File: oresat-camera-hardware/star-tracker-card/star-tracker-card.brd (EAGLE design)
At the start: 99.8 x 94.6 mm, 321 parts, among them J1 ORESAT-DEBUG-CONNECTOR-CARD, J100 DM3BT-DSF-PEJS, J101 3-1734592-64-1734592-0, J102 FTSH-105-XX-X-DV-K, J4 TFM-120-01-L-D-RA, Q1 MMBT2907, Q2 PMV45EN, Q3 DMP2240UDM, Q4 PMV45EN, Q5 MOSFET-PCH-SOT23-6, Q6 MOSFET-PCH-SOT23-6, U1 RCLAMP0504FB, U10 TLVH431, U11 TCAN330, U12 MIC842LYC5, U13 MIC842LYC5, U14 MAX4211FETE, U15 TPS62112, U16 MAX7310ATE, U17 25AAXX, U2 TPS2051CDBVR, U4 SN74LVC1G07DCK, U5 SN74LVC8T245MPWREPPW24-M, U6 CLVCH16T245MDGGREP, U7 OSD3358-512M-BSM, U8 TLV70028QDDCRQ1, U9 TCA9509DGKRDGK8-M, Y1 24MHz, Y2 ABS07-32.768KHZ-T

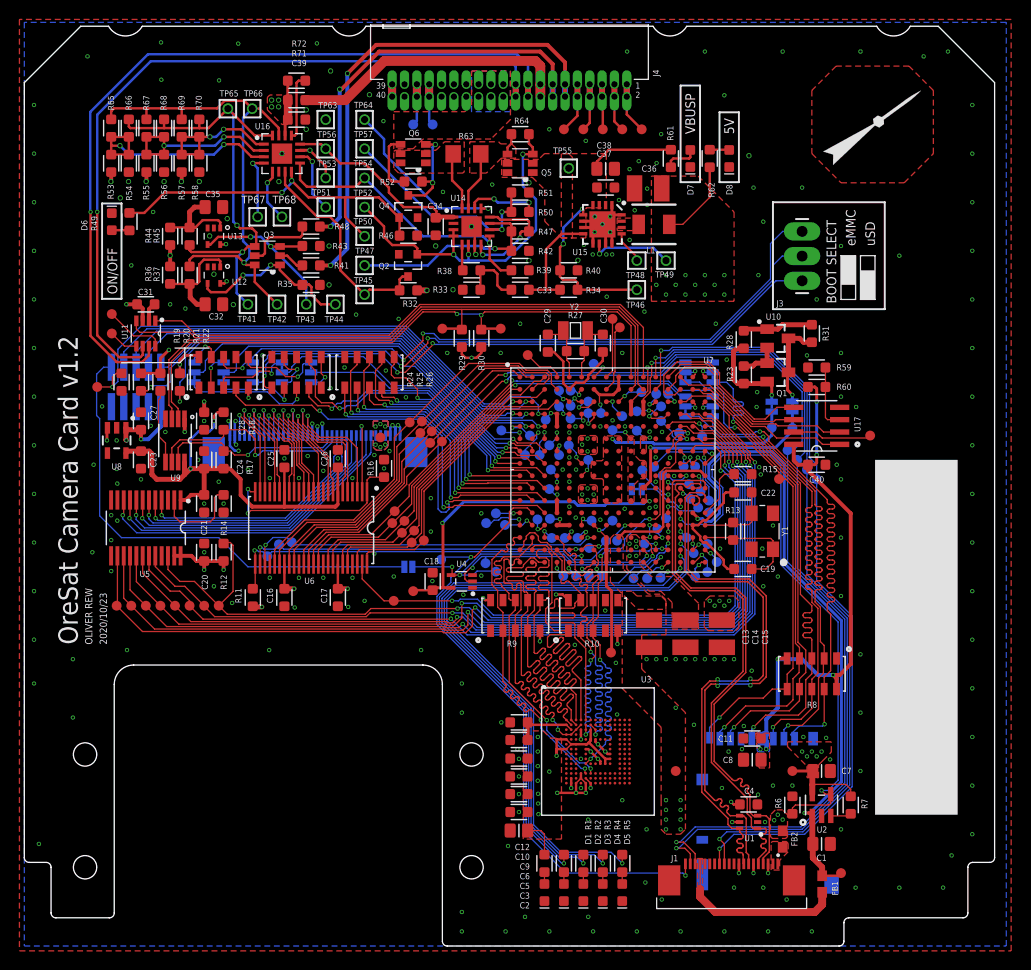
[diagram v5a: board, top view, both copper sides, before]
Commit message: added ESD protection to I2C0 and EEPROM_WP
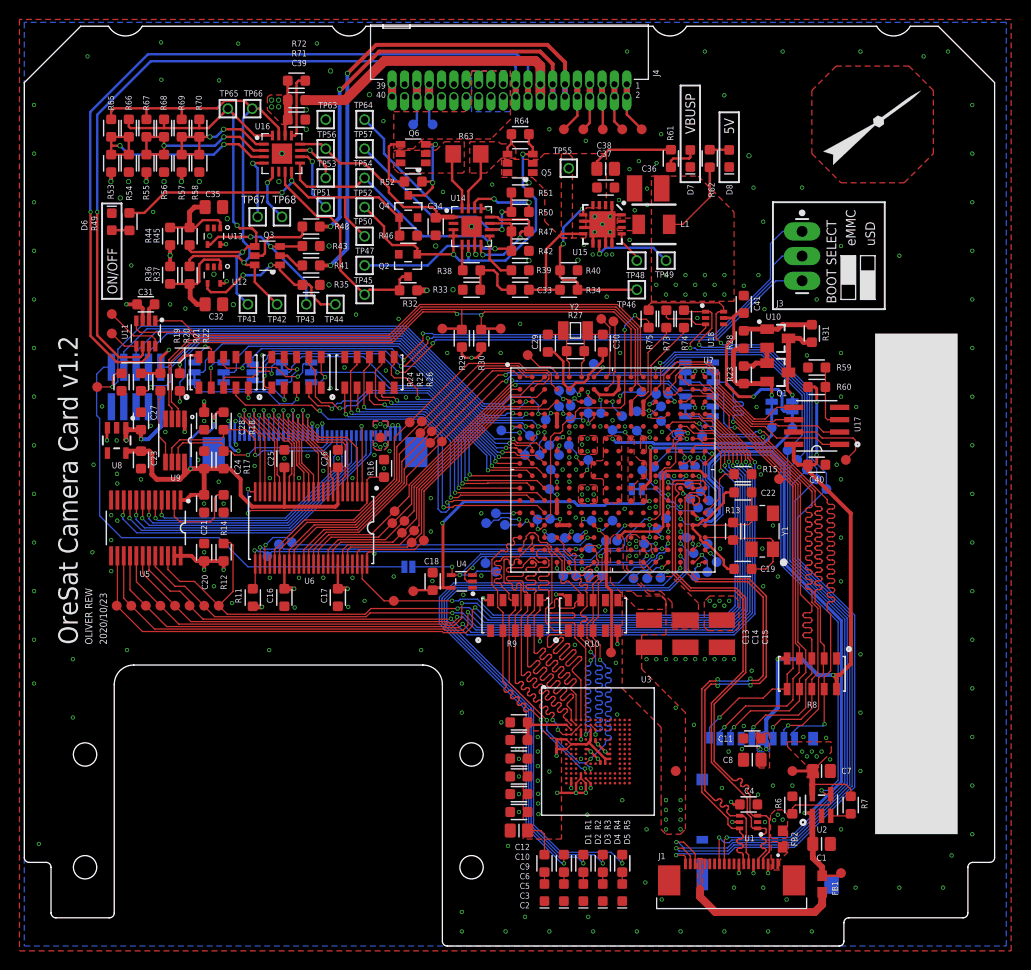
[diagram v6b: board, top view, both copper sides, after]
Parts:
- added C41: 0.1uF, oresat-rcl:.0603-A
- added R73, R74, R75: 100, oresat-rcl:.0603-A
- added U18: RCLAMP0504FB, U-Semtec-RCLAMP0504FB:SC70-6
- JP107: value JUMPER-SMT_3_NO_NO_SILK -> JUMPER-SMT_3_NO_SILK; device SparkFun-Jumpers:SMT-JUMPER_3_0-NO_TRACE_NO-SILK -> SparkFun-Jumpers:SMT-JUMPER_3_NO_SILK
- moved TP112 40.3 mm to (82.5, 47.0)
- moved TP69 3.54 mm to (84.5, 50.0)
- moved TP142 2.83 mm to (79.5, 50.0)
- moved TP146 2.83 mm to (78.5, 51.0)
- moved TP151 2.83 mm to (81.5, 48.0)
- moved TP155 2.83 mm to (80.5, 49.0)
- moved TP39 1.16 mm to (59.3, 64.5)
- moved TP38 0.91 mm to (60.6, 64.2)
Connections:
- removed net N$32: C18.1, JP104.1, TP14.P$1, TP164.P$1, U4.5, U7.K11, U7.L11
- new net 3.3VA: C18.1, C41.1, JP104.1, TP14.P$1, TP164.P$1, U18.5, U4.5, U7.K11, U7.L11
- new net N$114: R74.2, U7.C11, U7.D11
- new net N$115: R75.2, U7.M2
- new net N$116: R73.2, U7.C10, U7.D10
- net EEPROM_WP: now also R75.1, U18.6; no longer U7.M2
- net GND: now also C41.2, U18.2
- net I2C0_SCL: now also R73.1, U18.3; no longer U7.C10, U7.D10
- net I2C0_SDA: now also R74.1, U18.1; no longer U7.C11, U7.D11
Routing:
- net 3.3VA: track 0.00 -> 75.0 mm, vias 0 -> 4
- net N$32: track 56.0 -> 0.00 mm, vias 3 -> 0
- net N$115: track 0.00 -> 31.8 mm, vias 0 -> 2
- net EEPROM_WP: track 65.5 -> 92.5 mm
- net N$116: track 0.00 -> 10.8 mm
- net N$114: track 0.00 -> 10.6 mm
- net UART0_RX: track 80.5 -> 78.5 mm
- net I2C0_SDA: track 89.4 -> 87.9 mm
- net I2C0_SCL: track 90.9 -> 89.7 mm
- net N$111: track 8.22 -> 9.13 mm
- net N$68: track 2.98 -> 2.23 mm
- net GND: vias 291 -> 290
- added copper zone on layer 1, net 3.3VA
- removed copper zone on layer 1, net N$32

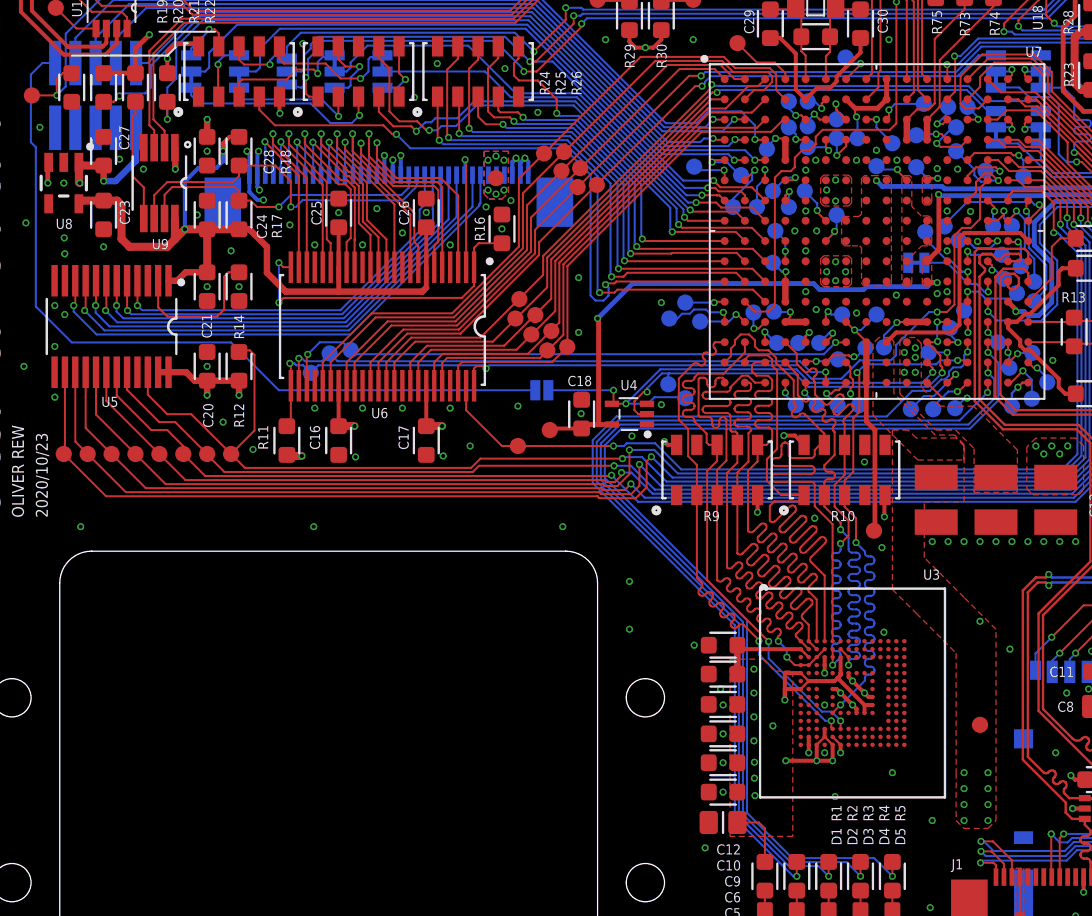
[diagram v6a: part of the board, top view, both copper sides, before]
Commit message: chore: a couple updates from design review
- add DXF layer for board outline footprint
- remove copper restrict from under camera mounts
- move FFC x-0.4mm to align with camera board(was off previously)
- add parts for I2C0 ESD circuit to BOM
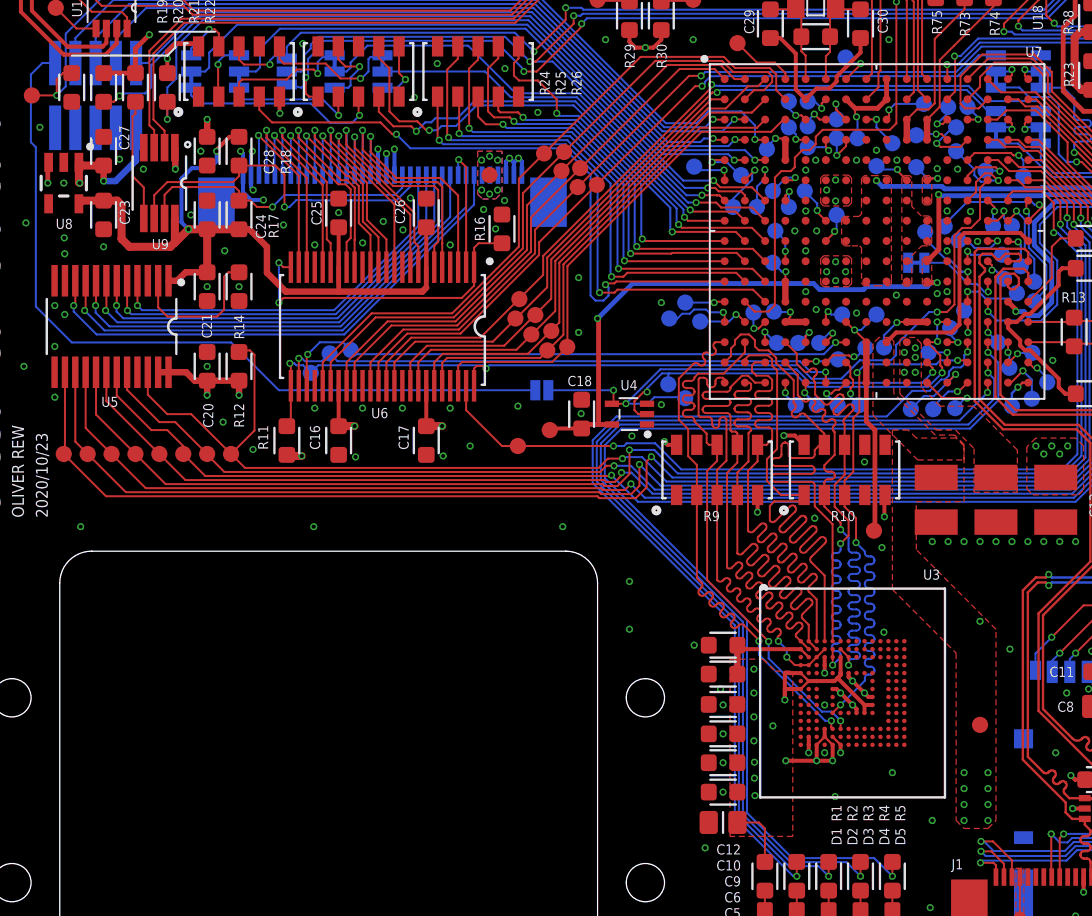
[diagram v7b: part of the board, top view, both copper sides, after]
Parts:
- moved U$2 1.17 mm to (10.2, 21.2)
- moved TP25 0.45 mm to (36.2, 52.5)
- moved J101 0.40 mm to (29.5, 52.5)
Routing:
- net GND: track 44.9 -> 46.5 mm
- net D5_E: track 11.7 -> 12.7 mm
- net VSYNC_E: track 10.9 -> 11.8 mm
- net PIXCLK_E: track 11.1 -> 12.0 mm
- net D9_E: track 13.4 -> 14.4 mm
- net D7_E: track 11.6 -> 12.6 mm
- net D1_E: track 11.4 -> 12.4 mm
- net D11_E: track 13.6 -> 14.5 mm
- net D3_E: track 11.5 -> 12.5 mm
- net HSYNC_E: track 11.9 -> 12.5 mm
- net D6_E: track 12.1 -> 12.7 mm
- net D4_E: track 12.5 -> 13.1 mm
- net D2_E: track 12.5 -> 13.1 mm
- net D10_E: track 14.4 -> 15.0 mm
- net D0_E: track 12.5 -> 13.1 mm
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
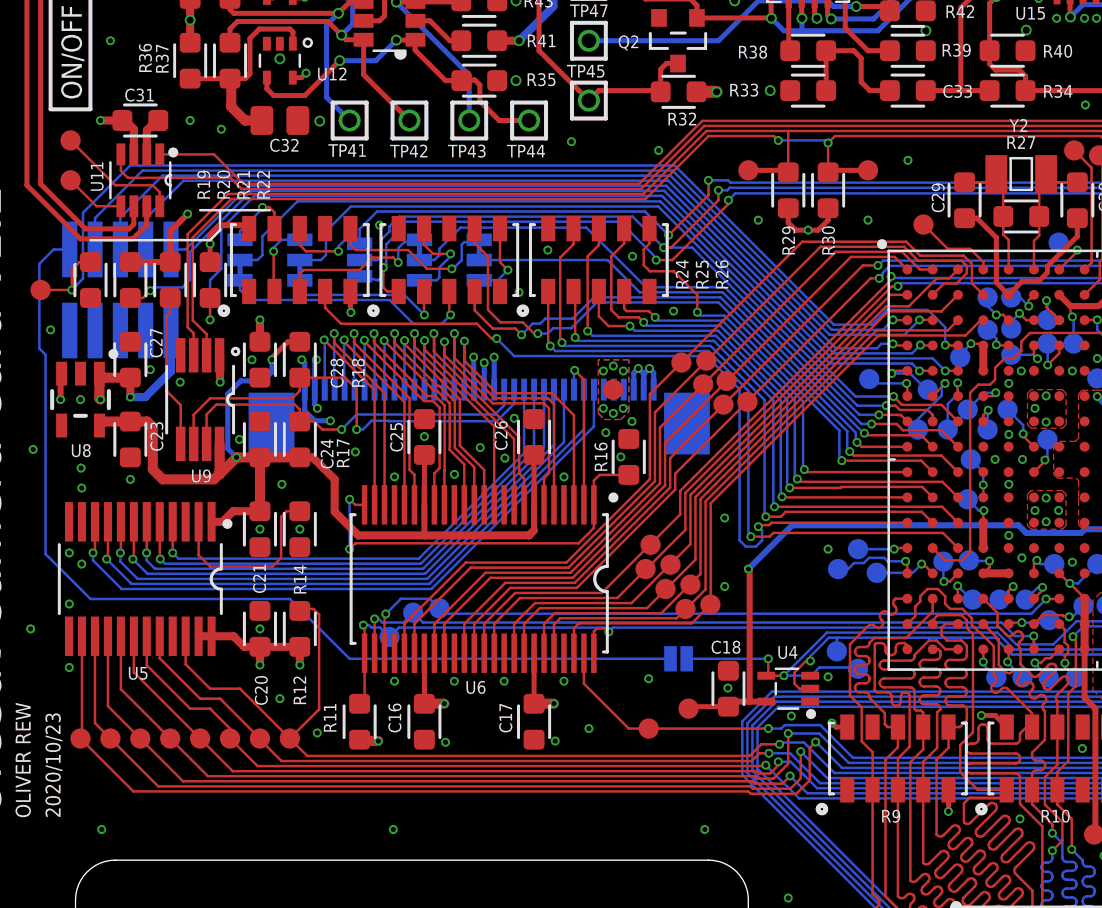
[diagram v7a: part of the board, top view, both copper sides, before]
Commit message: added a couple bulk caps on 3.3v line for camera
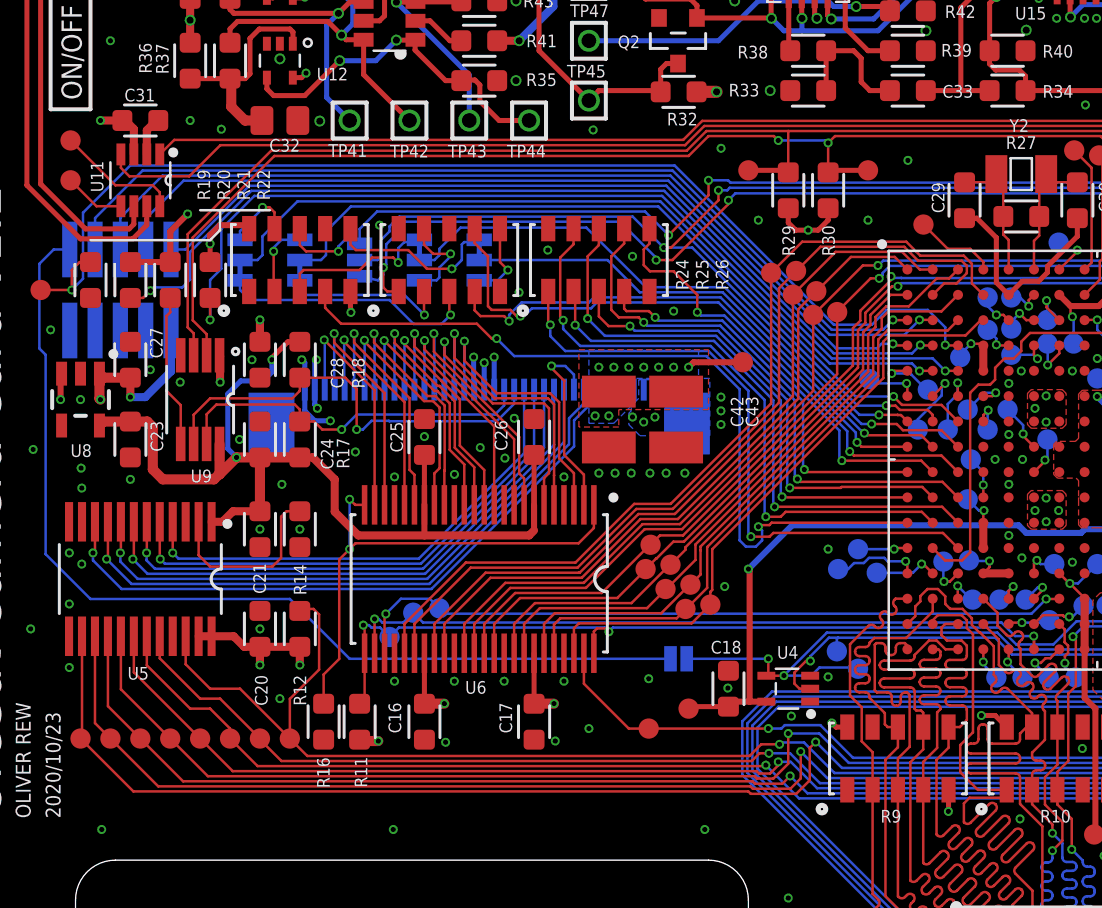
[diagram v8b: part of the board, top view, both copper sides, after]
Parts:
- added C42, C43: 22uF, oresat-rcl:C1210
- moved R16 20.3 mm to (21.7, 35.8), turned to 270 degrees
- moved TP25 6.64 mm to (42.7, 53.9)
- moved TP23 6.36 mm to (46.2, 56.2)
- moved TP24 6.36 mm to (47.5, 56.4)
- moved TP26 6.36 mm to (45.2, 57.3)
- moved TP27 6.36 mm to (46.4, 57.4)
- moved TP28 6.36 mm to (44.1, 58.4)
- moved TP29 6.36 mm to (45.4, 58.5)
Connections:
- net 3.3V: now also C42.1, C43.1
- net GND: now also C42.2, C43.2
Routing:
- net N$19: track 20.3 -> 25.5 mm
- net GND: track 46.5 -> 41.9 mm, vias 290 -> 295
- net 3.3V: track 131.1 -> 134.0 mm, vias 46 -> 49
- net FLASH_E: track 7.92 -> 9.70 mm
- net D6_I: track 42.2 -> 43.7 mm
- net D5_I: track 36.2 -> 37.5 mm
- net D4_I: track 33.9 -> 35.2 mm
- net D2_I: track 48.8 -> 50.1 mm
- net N$12: track 58.0 -> 56.8 mm
- net D3_I: track 53.4 -> 54.4 mm
- net PIXCLK_I: track 43.0 -> 44.0 mm
- net N$586: track 33.1 -> 32.3 mm
- net N$11: track 61.5 -> 60.9 mm
- net D11_I: track 31.4 -> 30.8 mm
